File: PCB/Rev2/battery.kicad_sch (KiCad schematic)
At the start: 13 parts, among them U3 TP4057, U4 TPS2116DRL, U5 TPS2116DRL

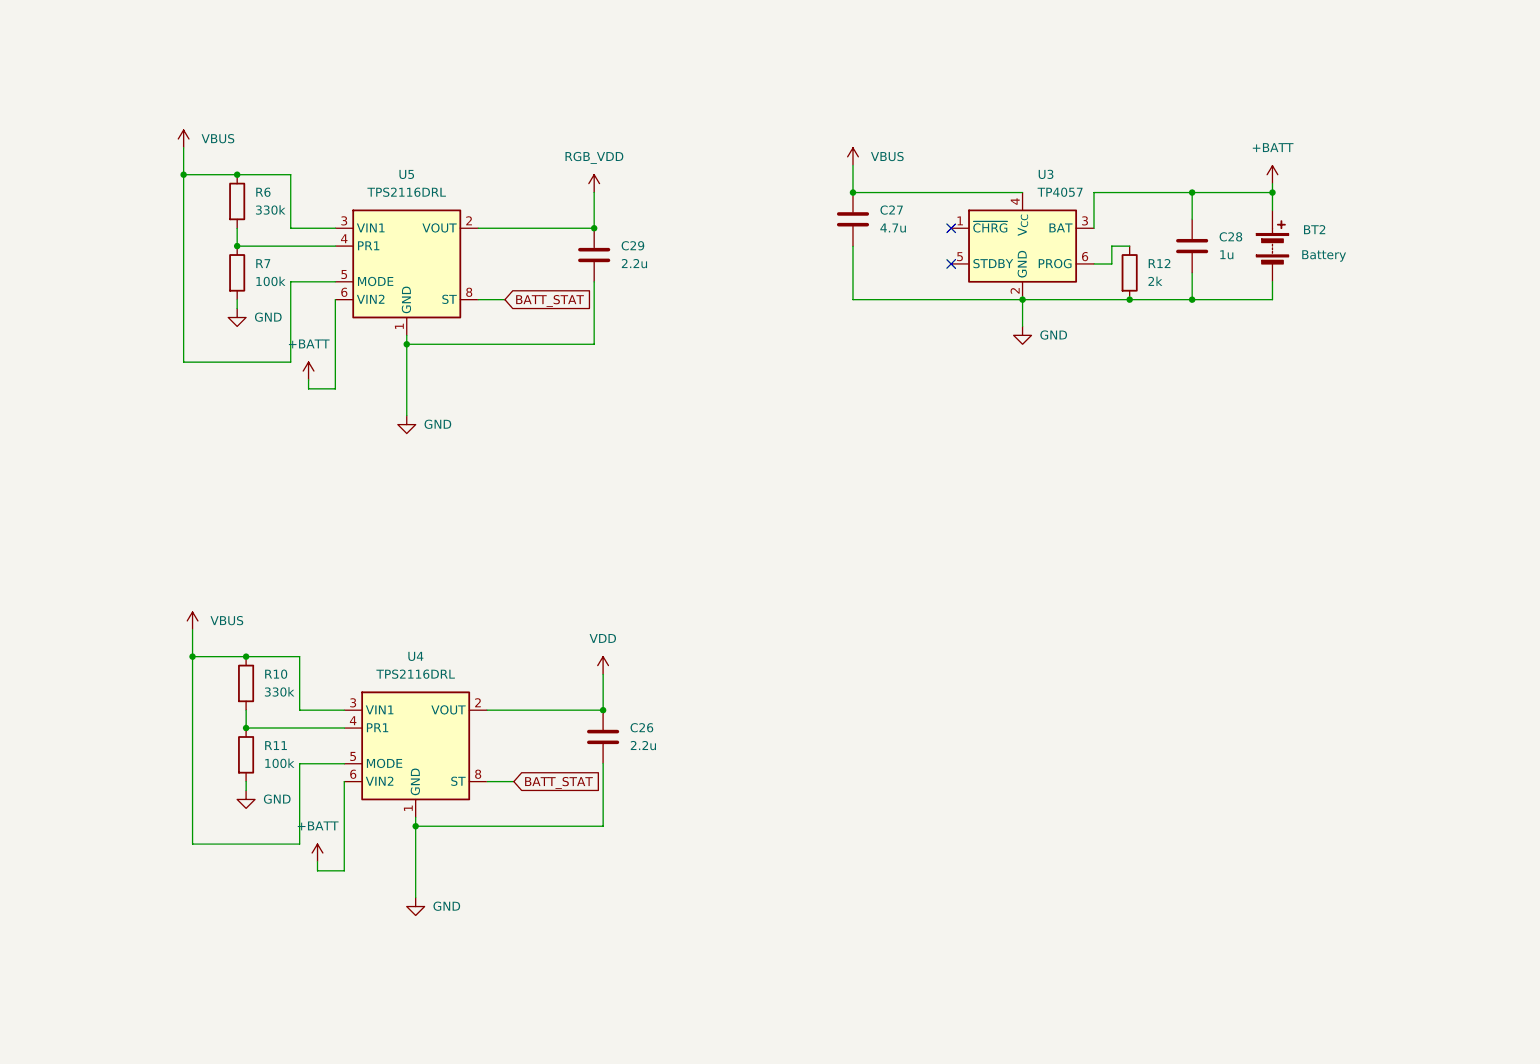
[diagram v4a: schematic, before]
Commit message: 电源模块布局及drc
修改52840的vddh，将batt修改为vdd，TPS2116DRL布局与简单drc，rgb_vdd布局仍需修改
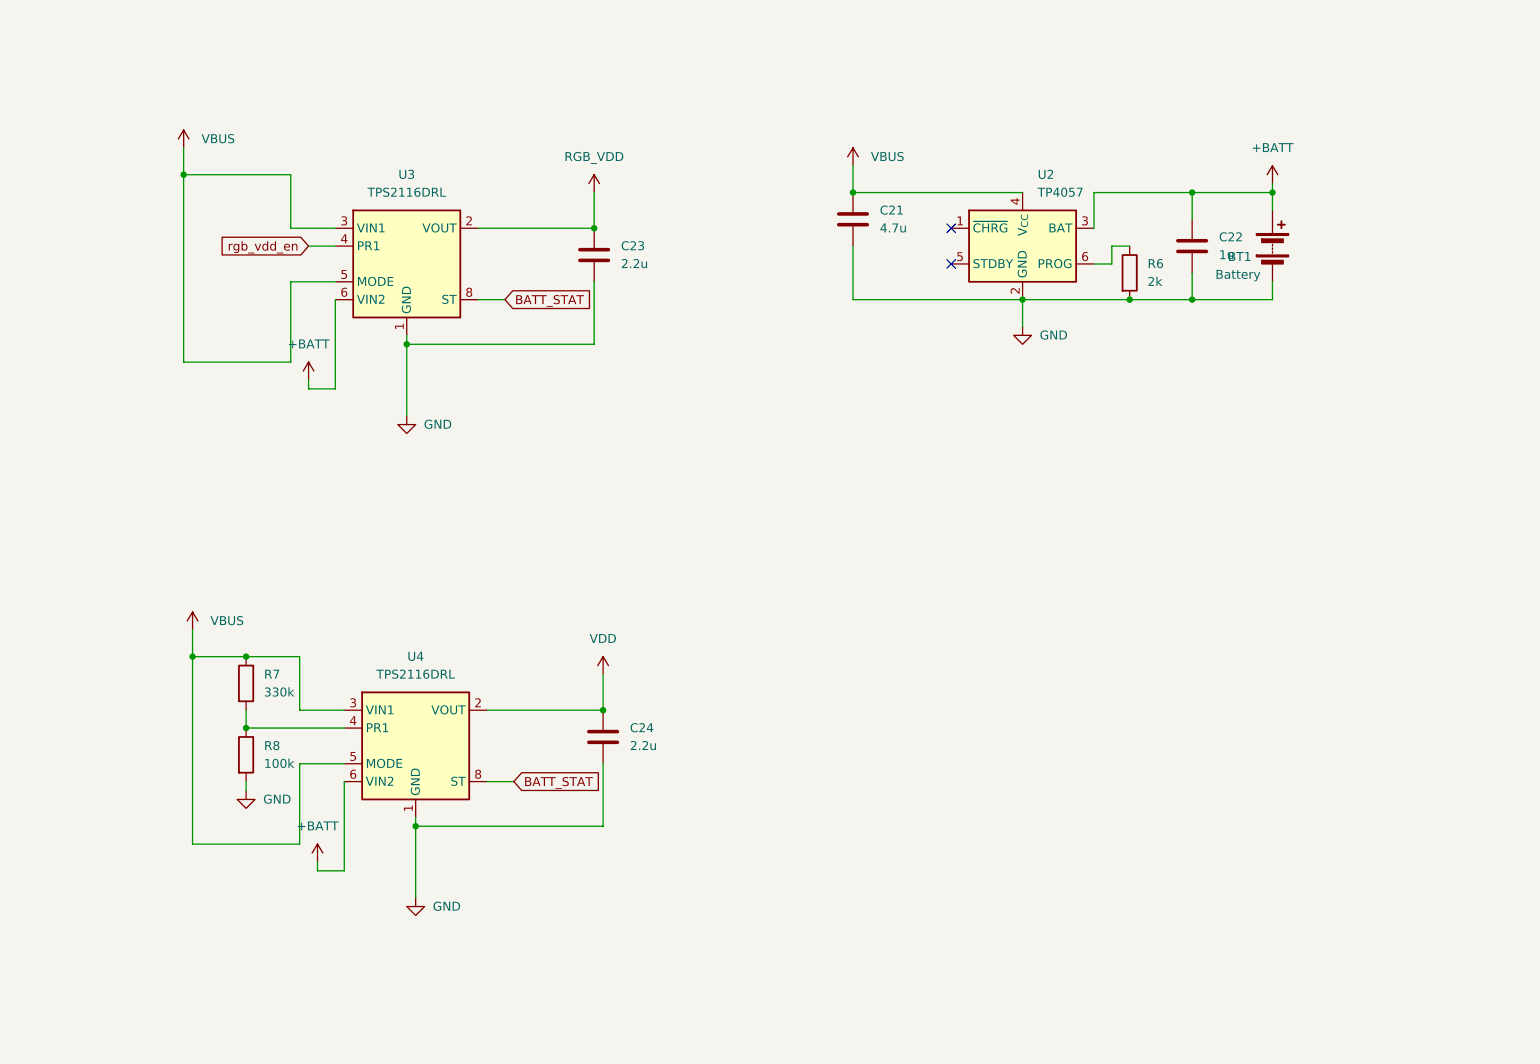
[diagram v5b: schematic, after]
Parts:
- removed BT2: Battery, Connector_Molex:Molex_PicoBlade_53261-0271_1x02-1MP_P1.25mm_Horizontal, symbol Device:Battery
- removed R6: 330k, Resistor_SMD:R_0402_1005Metric, symbol Device:R
- removed R7: 100k, Resistor_SMD:R_0402_1005Metric, symbol Device:R
- added BT1: Battery, Connector_Molex:Molex_Panelmate_53780-0270_1x02-1MP_P1.25mm_Horizontal, symbol Device:Battery
- renumbered C27 to C21, C28 to C22, C29 to C23, C26 to C24, R12 to R6, R10 to R7, R11 to R8, U3 to U2, U5 to U3
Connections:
- net +BATT: now also BT1.1 (+)
- net GND: now also BT1.2 (-)
- net rgb_vdd_en: now reaches U3.4 (PR1)

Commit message: sc2最终审核（nayat）
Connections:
- net BATT_STAT: no longer U3.8 (ST), U4.8 (ST)
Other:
- note added: "Lithium battery charging module"
- note added: "MCU power supply chip select module"
- note added: "RGB power supply chip select module"
- moved on the sheet: BT1, C21, C22, C23, C24, R6, R7, R8, U2, U3, U4

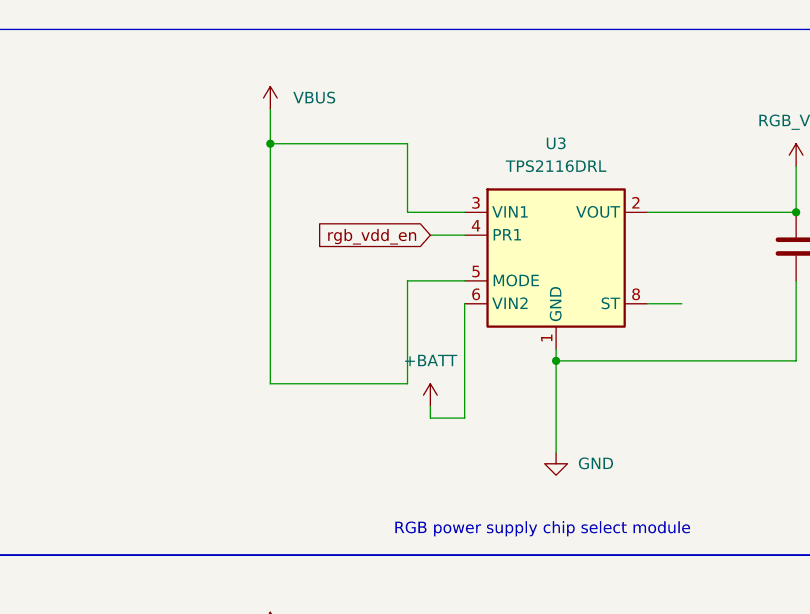
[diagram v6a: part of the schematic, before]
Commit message: 电池部分修改及drc
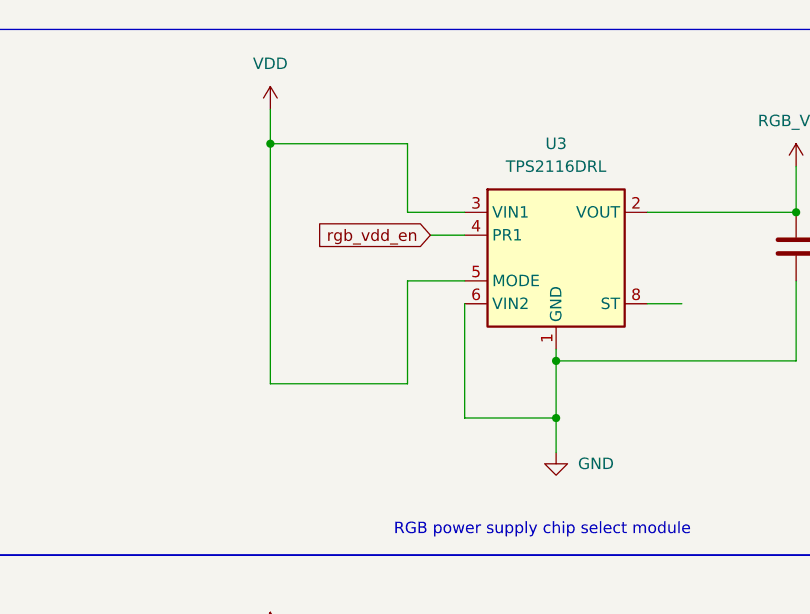
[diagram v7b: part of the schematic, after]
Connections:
- net +BATT: no longer U3.6 (VIN2)
- net GND: now also U3.6 (VIN2)
- net VBUS: no longer U3.3 (VIN1), U3.5 (MODE)
- net VDD: now also U3.3 (VIN1), U3.5 (MODE)
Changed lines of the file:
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@@
+	)
+	(junction
+		(at 171.45 55.88)
+		(diameter 0)
+		(color 0 0 0 0)
 	)
 	(junction
@@
 	(wire
 		(pts
+			(xy 171.45 55.88) (xy 171.45 59.69)
+		)
+		(stroke
+			(width 0)
+			(type default)
+		)
+	)
+	(wire
+		(pts
 			(xy 154.94 52.07) (xy 154.94 40.64)
 		)
@@
 	(wire
 		(pts
-			(xy 157.48 55.88) (xy 161.29 55.88)
-		)
-		(stroke
-			(width 0)
-			(type default)
-		)
-	)
-	(wire
-		(pts
 			(xy 154.94 25.4) (xy 154.94 33.02)
 		)
@@
 	(wire
 		(pts
-			(xy 157.48 55.88) (xy 157.48 54.61)
-		)
-		(stroke
-			(width 0)
-			(type default)
-		)
-	)
-	(wire
-		(pts
-			(xy 171.45 49.53) (xy 171.45 59.69)
+			(xy 171.45 49.53) (xy 171.45 55.88)
 		)
 		(stroke
@@
 	(wire
 		(pts
+			(xy 161.29 43.18) (xy 161.29 55.88)
+		)
+		(stroke
+			(width 0)
+			(type default)
+		)
+	)
+	(wire
+		(pts
+			(xy 161.29 55.88) (xy 171.45 55.88)
+		)
+		(stroke
+			(width 0)
+			(type default)
+		)
+	)
+	(wire
+		(pts
 			(xy 35.56 36.83) (xy 59.69 36.83)
-		)
-		(stroke
-			(width 0)
-			(type default)
-		)
-	)
-	(wire
-		(pts
-			(xy 161.29 43.18) (xy 161.29 55.88)
 		)
 		(stroke
@@
 	)
 	(symbol
-		(lib_id "power:VBUS")
-		(at 139.7 21.59 0)
-		(unit 1)
-		(exclude_from_sim no)
-		(in_bom yes)
-		(on_board yes)
-		(dnp no)
-		(fields_autoplaced yes)
-		(property "Reference" "#PWR018"
-			(at 139.7 25.4 0)
-			(effects
-				(font
-					(size 1.27 1.27)
-				)
-				(hide yes)
-			)
-		)
-		(property "Value" "VBUS"
-			(at 142.24 20.3199 0)
-			(effects
-				(font
-					(size 1.27 1.27)
-				)
-				(justify left)
-			)
-		)
-		(property "Footprint" ""
-			(at 139.7 21.59 0)
-			(effects
-				(font
-					(size 1.27 1.27)
-				)
-				(hide yes)
-			)
-		)
-		(property "Datasheet" ""
-			(at 139.7 21.59 0)
-			(effects
-				(font
-					(size 1.27 1.27)
-				)
-				(hide yes)
-			)
-		)
-		(property "Description" "Power symbol creates a global label with name \"VBUS\""
-			(at 139.7 21.59 0)
-			(effects
-				(font
-					(size 1.27 1.27)
-				)
-				(hide yes)
-			)
-		)
-		(pin "1"
-		)
-		(instances
-			(project "PH60-SC_Rev2"
-				(path "/dca0f898-8fdb-4522-a51d-f4f4238906e7/65afedf5-5b27-4d53-9ad9-9264a927261c"
-					(reference "#PWR018")
-					(unit 1)
-				)
-			)
-		)
-	)
-	(symbol
 		(lib_id "power:GND")
 		(at 59.69 55.88 0)
@@
 	)
 	(symbol
+		(lib_id "power:VDD")
+		(at 139.7 21.59 0)
+		(unit 1)
+		(exclude_from_sim no)
+		(in_bom yes)
+		(on_board yes)
+		(dnp no)
+		(fields_autoplaced yes)
+		(property "Reference" "#PWR018"
+			(at 139.7 25.4 0)
+			(effects
+				(font
+					(size 1.27 1.27)
+				)
+				(hide yes)
+			)
+		)
+		(property "Value" "VDD"
+			(at 139.7 16.51 0)
+			(effects
+				(font
+					(size 1.27 1.27)
+				)
+			)
+		)
+		(property "Footprint" ""
+			(at 139.7 21.59 0)
+			(effects
+				(font
+					(size 1.27 1.27)
+				)
+				(hide yes)
+			)
+		)
+		(property "Datasheet" ""
+			(at 139.7 21.59 0)
+			(effects
+				(font
+					(size 1.27 1.27)
+				)
+				(hide yes)
+			)
+		)
+		(property "Description" "Power symbol creates a global label with name \"VDD\""
+			(at 139.7 21.59 0)
+			(effects
+				(font
+					(size 1.27 1.27)
+				)
+				(hide yes)
+			)
+		)
+		(pin "1"
+		)
+		(instances
+			(project "PH60-SC_Rev2"
+				(path "/dca0f898-8fdb-4522-a51d-f4f4238906e7/65afedf5-5b27-4d53-9ad9-9264a927261c"
+					(reference "#PWR018")
+					(unit 1)
+				)
+			)
+		)
+	)
+	(symbol
 		(lib_id "power:+BATT")
 		(at 157.48 113.03 0)
@@
 					(unit 1)
 				)
-			)
-		)
-	)
-	(symbol
-		(lib_id "power:+BATT")
-		(at 157.48 54.61 0)
-		(unit 1)
-		(exclude_from_sim no)
-		(in_bom yes)
-		(on_board yes)
-		(dnp no)
-		(fields_autoplaced yes)
-		(property "Reference" "#PWR023"
-			(at 157.48 58.42 0)
-			(effects
-				(font
-					(size 1.27 1.27)
-				)
-				(hide yes)
-			)
-		)
-		(property "Value" "+BATT"
-			(at 157.48 49.53 0)
-			(effects
-				(font
-					(size 1.27 1.27)
-				)
-			)
-		)
-		(property "Footprint" ""
-			(at 157.48 54.61 0)
-			(effects
-				(font
-					(size 1.27 1.27)
-				)
-				(hide yes)
-			)
-		)
-		(property "Datasheet" ""
-			(at 157.48 54.61 0)
-			(effects
-				(font
-					(size 1.27 1.27)
-				)
-				(hide yes)
-			)
-		)
-		(property "Description" "Power symbol creates a global label with name \"+BATT\""
-			(at 157.48 54.61 0)
-			(effects
-				(font
-					(size 1.27 1.27)
-				)
-				(hide yes)
-			)
-		)
-		(pin "1"
-		)
-		(instances
-			(project "PH60-SC_Rev2"
-				(path "/dca0f898-8fdb-4522-a51d-f4f4238906e7/65afedf5-5b27-4d53-9ad9-9264a927261c"
-					(reference "#PWR023")
-					(unit 1)
-				)
